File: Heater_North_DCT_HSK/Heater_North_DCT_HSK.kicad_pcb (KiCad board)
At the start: 2 copper layers, 53.3 x 57.1 mm, 5 parts, among them J1 North_Heater_1, J2 North_Heater_2, J3 Internal_Heater_DCT_HSK_Box

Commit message: See previous commit
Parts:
- J1: value North_Heater_1 -> NHB1
- J2: value North_Heater_2 -> NHB2
- J3: value Internal_Heater_DCT_HSK_Box -> North Heater
- moved G*** 41.5 mm to (134.6, 94.7)
- moved J3 5.10 mm to (141.0, 75.6)
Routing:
- net /HB_8: track 43.3 -> 0.00 mm
- net /HB_7: track 43.3 -> 0.00 mm
- net /HB_2: track 43.3 -> 2.43 mm
- net /HB_1: track 43.3 -> 5.27 mm
- net /HB_13: track 86.6 -> 76.3 mm
- net /HB_21: track 43.5 -> 37.6 mm
- net /HB_25: track 43.3 -> 38.1 mm
- net /HB_23: track 43.3 -> 38.1 mm
- net /HB_17: track 43.3 -> 38.1 mm
- net /HB_27: track 43.3 -> 38.1 mm
- net /HB_19: track 43.3 -> 38.1 mm
- net /HB_22: track 45.7 -> 40.7 mm
- net /HB_28: track 43.3 -> 39.6 mm
- net /HB_14: track 43.3 -> 39.6 mm
- net /HB_6: track 43.9 -> 47.5 mm
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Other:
- board text added: "From DCT"
- board text added: "Heater North Rev B Dennis H. Calderon 09/09/2023"
- board text removed: "Heater_North_DCT_HSK Dennis H. Calderon 10/21/2022"

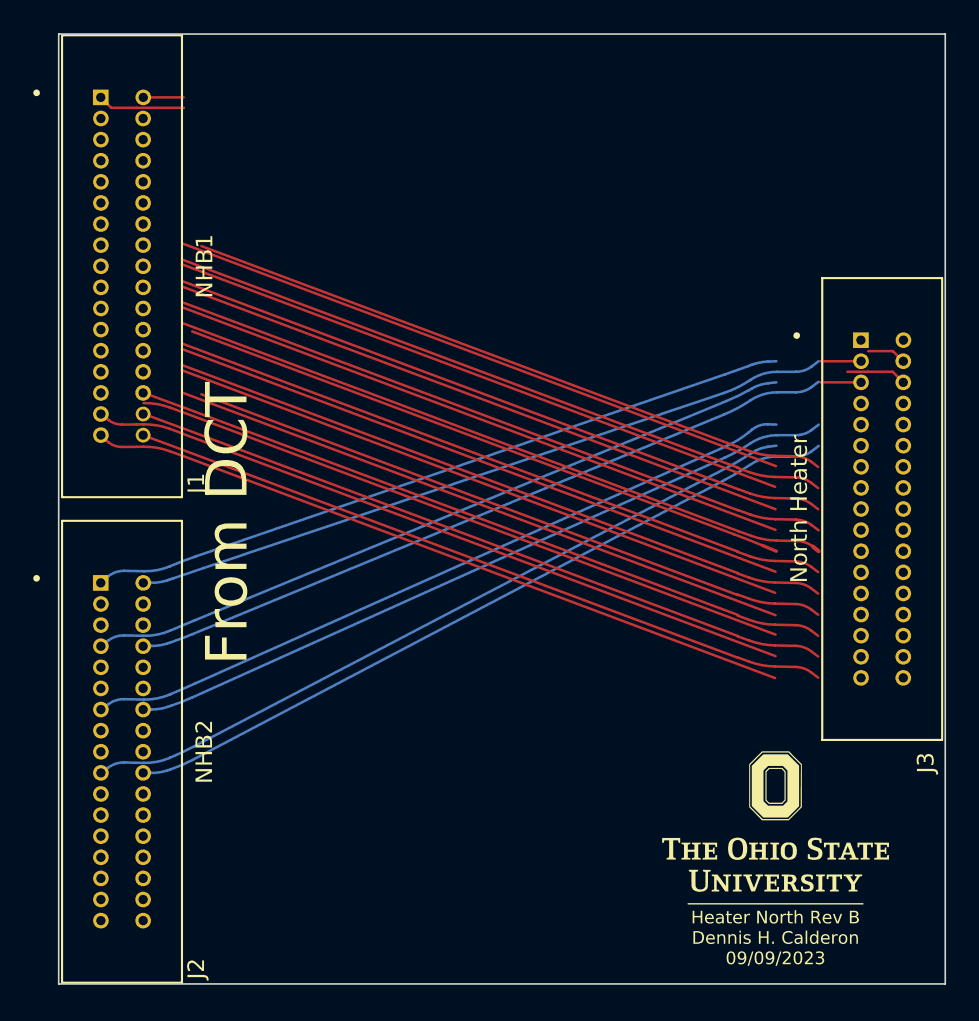
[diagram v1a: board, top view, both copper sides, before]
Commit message: Heater norths updated with large track width and mapping, as well as clear labels in schematic. Fits on same width PCB as original, depth is slightly increase and doesn't matter for front panel or box.
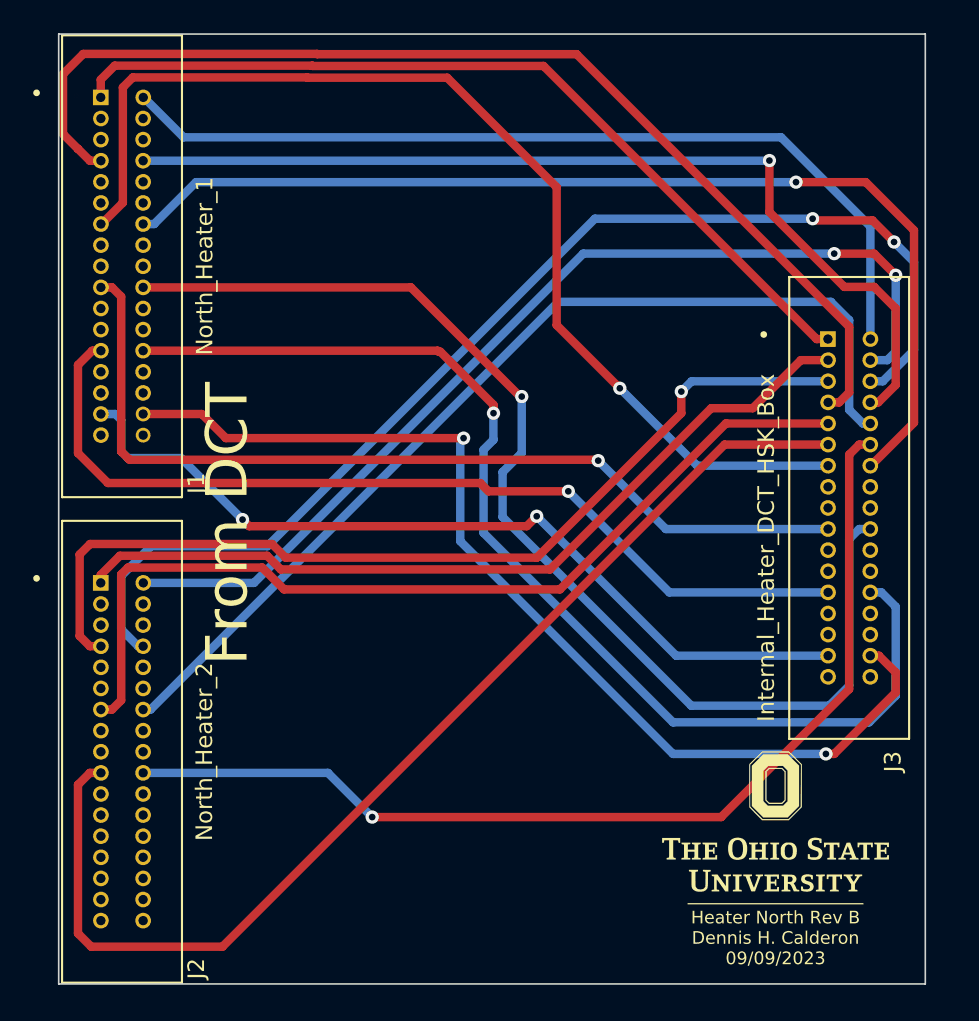
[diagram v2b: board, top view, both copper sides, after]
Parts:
- J1: value NHB1 -> North_Heater_1
- J2: value NHB2 -> North_Heater_2
- J3: value North Heater -> Internal_Heater_DCT_HSK_Box
- moved J3 1.99 mm to (139.0, 75.5)
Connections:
- net /HB_1 renamed /HB1_1
- net /HB_10 renamed /HB2_14
- net /HB_11 renamed /HB2_19
- net /HB_12 renamed /HB2_20
- net /HB_14 renamed /HB1_14
- net /HB_19 renamed /HB1_19
- net /HB_2 renamed /HB1_2
- net /HB_20 renamed /HB1_20
- net /HB_25 renamed /HB1_25
- net /HB_26 renamed /HB1_26
- net /HB_3 renamed /HB2_1
- net /HB_31 renamed /HB1_31
- net /HB_32 renamed /HB1_32
- net /HB_4 renamed /HB2_2
- net /HB_5 renamed /HB2_7
- net /HB_6 renamed /HB2_8
- net /HB_7 renamed /HB1_7
- net /HB_8 renamed /HB1_8
- net /HB_9 renamed /HB2_13
- J1 pad 13: /HB_13 -> /HB1_13
- J1 pad 15: /HB_13 -> unconnected-(J1-Pin_15-Pad15)
- J1 pad 16: /HB_16 -> unconnected-(J1-Pin_16-Pad16)
- J1 pad 17: /HB_17 -> unconnected-(J1-Pin_17-Pad17)
- J1 pad 18: /HB_18 -> unconnected-(J1-Pin_18-Pad18)
- J1 pad 21: /HB_21 -> unconnected-(J1-Pin_21-Pad21)
- J1 pad 22: /HB_22 -> unconnected-(J1-Pin_22-Pad22)
- J1 pad 23: /HB_23 -> unconnected-(J1-Pin_23-Pad23)
- J1 pad 24: /HB_24 -> unconnected-(J1-Pin_24-Pad24)
- J1 pad 27: /HB_27 -> unconnected-(J1-Pin_27-Pad27)
- J1 pad 28: /HB_28 -> unconnected-(J1-Pin_28-Pad28)
- J1 pad 29: /HB_29 -> unconnected-(J1-Pin_29-Pad29)
- J1 pad 30: /HB_30 -> unconnected-(J1-Pin_30-Pad30)
- J1 pad 33: /HB_33 -> unconnected-(J1-Pin_33-Pad33)
- J1 pad 34: /HB_34 -> unconnected-(J1-Pin_34-Pad34)
- J3 pad 13: /HB_13 -> /HB1_13
- J3 pad 15: /HB_15 -> unconnected-(J3-Pin_15-Pad15)
- J3 pad 16: /HB_16 -> unconnected-(J3-Pin_16-Pad16)
- J3 pad 17: /HB_17 -> unconnected-(J3-Pin_17-Pad17)
- J3 pad 18: /HB_18 -> unconnected-(J3-Pin_18-Pad18)
- J3 pad 21: /HB_21 -> unconnected-(J3-Pin_21-Pad21)
- J3 pad 22: /HB_22 -> unconnected-(J3-Pin_22-Pad22)
- J3 pad 23: /HB_23 -> unconnected-(J3-Pin_23-Pad23)
- J3 pad 24: /HB_24 -> unconnected-(J3-Pin_24-Pad24)
- J3 pad 27: /HB_27 -> unconnected-(J3-Pin_27-Pad27)
- J3 pad 28: /HB_28 -> unconnected-(J3-Pin_28-Pad28)
- J3 pad 29: /HB_29 -> unconnected-(J3-Pin_29-Pad29)
- J3 pad 30: /HB_30 -> unconnected-(J3-Pin_30-Pad30)
- J3 pad 33: /HB_33 -> unconnected-(J3-Pin_33-Pad33)
- J3 pad 34: /HB_34 -> unconnected-(J3-Pin_34-Pad34)
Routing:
- net /HB_13: track 76.3 -> 0.00 mm
- net /HB1_7: track 0.00 -> 66.6 mm
- net /HB1_13: track 0.00 -> 66.0 mm, vias 0 -> 1
- net /HB1_8: track 0.00 -> 57.4 mm, vias 0 -> 1
- net /HB1_2: track 2.43 -> 53.7 mm
- net /HB1_1: track 5.27 -> 52.0 mm
- net /HB_30: track 43.3 -> 0.00 mm
- net /HB_34: track 43.3 -> 0.00 mm
- net /HB_33: track 43.3 -> 0.00 mm
- net /HB_24: track 40.8 -> 0.00 mm
- net /HB_18: track 40.8 -> 0.00 mm
- net /HB_16: track 40.8 -> 0.00 mm
- net /HB_22: track 40.7 -> 0.00 mm
- net /HB_29: track 40.6 -> 0.00 mm
- net /HB_28: track 39.6 -> 0.00 mm
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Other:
- board size 53.3 x 57.1 mm -> 52.1 x 57.1 mm

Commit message: Added mounting holes for North Temp. South Temp board updated based off K. McBride pull request.
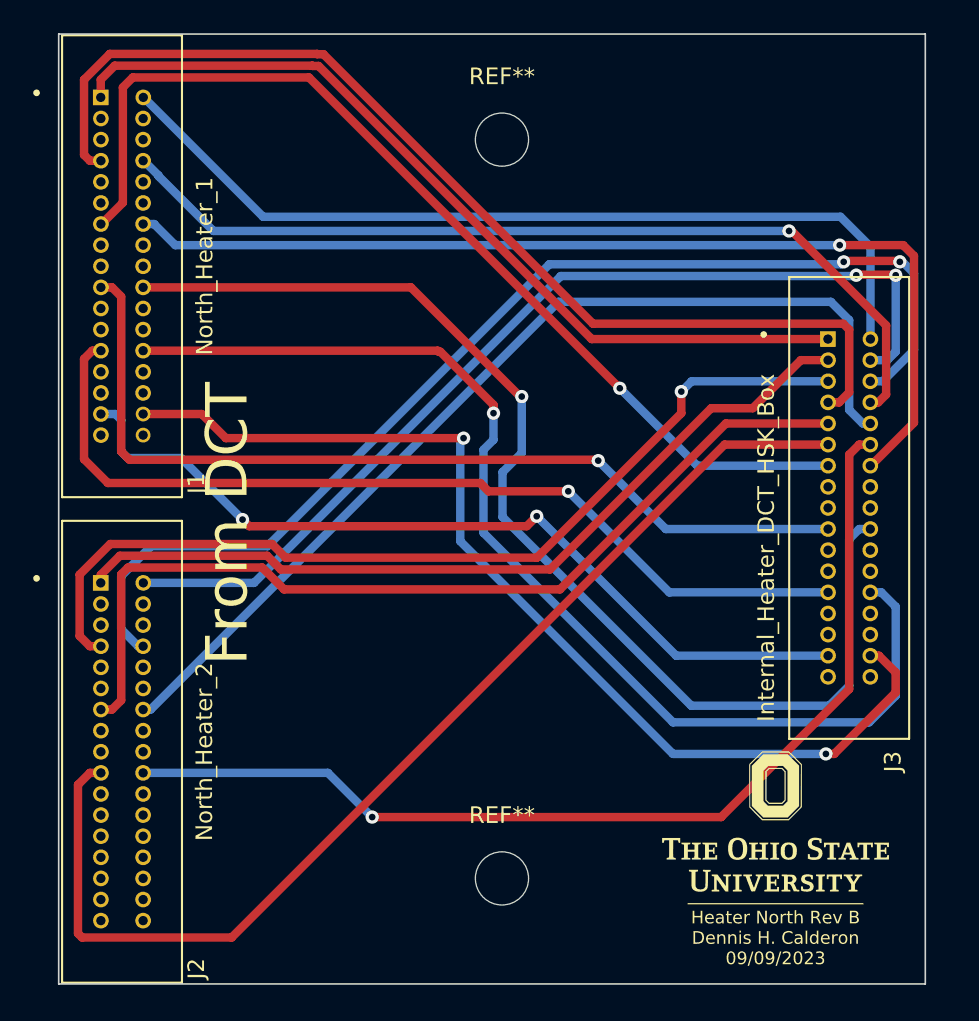
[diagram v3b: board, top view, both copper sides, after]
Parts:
- added REF**: MountingHole_3.2mm_M3_DIN965, MountingHole:MountingHole_3.2mm_M3_DIN965, F.Cu at (118.1, 53.3)
- added REF**: MountingHole_3.2mm_M3_DIN965, MountingHole:MountingHole_3.2mm_M3_DIN965, F.Cu at (118.1, 97.8)
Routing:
- net /HB1_13: track 66.0 -> 61.1 mm
- net /HB1_8: track 57.4 -> 54.1 mm
- net /HB1_14: track 63.9 -> 60.9 mm
- net /HB2_8: track 71.3 -> 68.9 mm
- net /HB1_7: track 66.6 -> 64.5 mm
- net /HB2_2: track 60.4 -> 59.6 mm
- net /HB2_7: track 57.2 -> 56.5 mm
- net /HB1_2: track 53.7 -> 53.0 mm
